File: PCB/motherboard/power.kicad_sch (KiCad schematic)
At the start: 0 parts

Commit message: started power schematic of pcb
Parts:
- added C1, C2, C3: C, symbol Device:C
- added C4: 100n, symbol Device:C
- added C5: 10u, symbol Device:C
- added L1: L, symbol Device:L
- added R1, R2, R3, R4, R6: R, symbol Device:R
- added U1: TPS54140ADGQR, DGQ10_1P88X1P57_TEX, symbol tps54140:TPS54140ADGQR
- added U2: PTPS259830LNRGER, VQFN24_RGE_TEX, symbol tps25983:PTPS259830LNRGER
- added U3: AP2112K-3.3TRG1, SOT_RG1_DIO, symbol AP2112K-3.3TRG1:AP2112K-3.3TRG1
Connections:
- new net: L1.1, U1.10 (PH)
- new net: R3.2, R4.1, U2.12 (OVLO)
- new net: C1.1, U2.7 (ITIMER)
- new net: R6.1, U2.8 (ILIM)
- new net: R2.2, R3.1, U2.6 (EN/UVLO)
- new net: C3.1, U2.15 (DVDT/_BGATE)
- new net: C2.1, U2.10 (RETRY_DLY)
- new net +24V: C5.1, U1.2 (VIN), U2.17 (OUT), U2.18 (OUT), U2.19 (OUT), U2.20 (OUT), U2.21 (OUT), U2.22 (OUT), U2.23 (OUT), U2.24 (OUT)
- new net +24V_UNPROTECTED: C4.1, R2.1, U2.1 (IN), U2.16 (IN), U2.2 (IN), U2.25 (IN), U2.3 (IN)
- new net +3.3V: U3.5 (VOUT)
- new net +5V: L1.2, U3.1 (VIN)
- new net GND: C1.2, C2.2, C3.2, C4.2, C5.2, R1.2, R4.2, R6.2, U1.9 (GND), U2.11 (NRETRY), U2.14 (GND), U2.26 (GND), U2.4 (GND), U2.5 (GND), U3.2 (GND)
- new net IMON: R1.1, U2.9 (IMON)
- new net PG_EFUSE: U2.13 (PG)
- no-connect marks 0 -> 1
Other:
- note added: "BUCK 24V TO 5V"
- note added: "EFUSE"
- note added: "LDO 5V to 3V3"

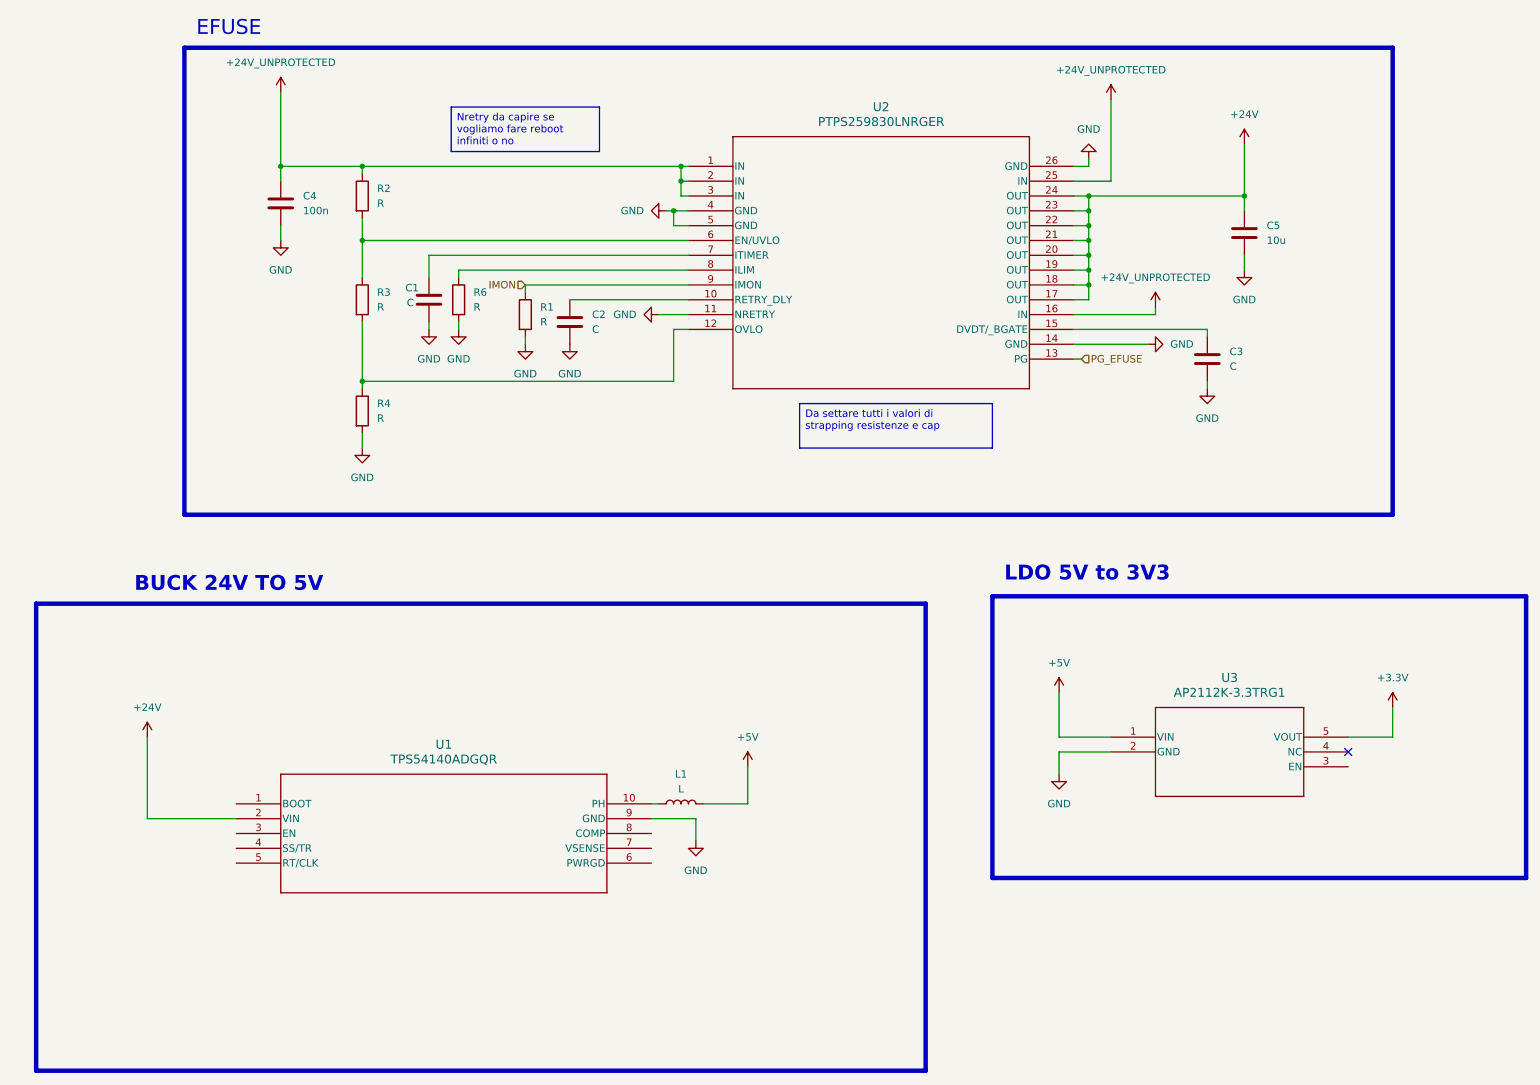
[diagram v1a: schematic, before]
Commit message: updated sch power
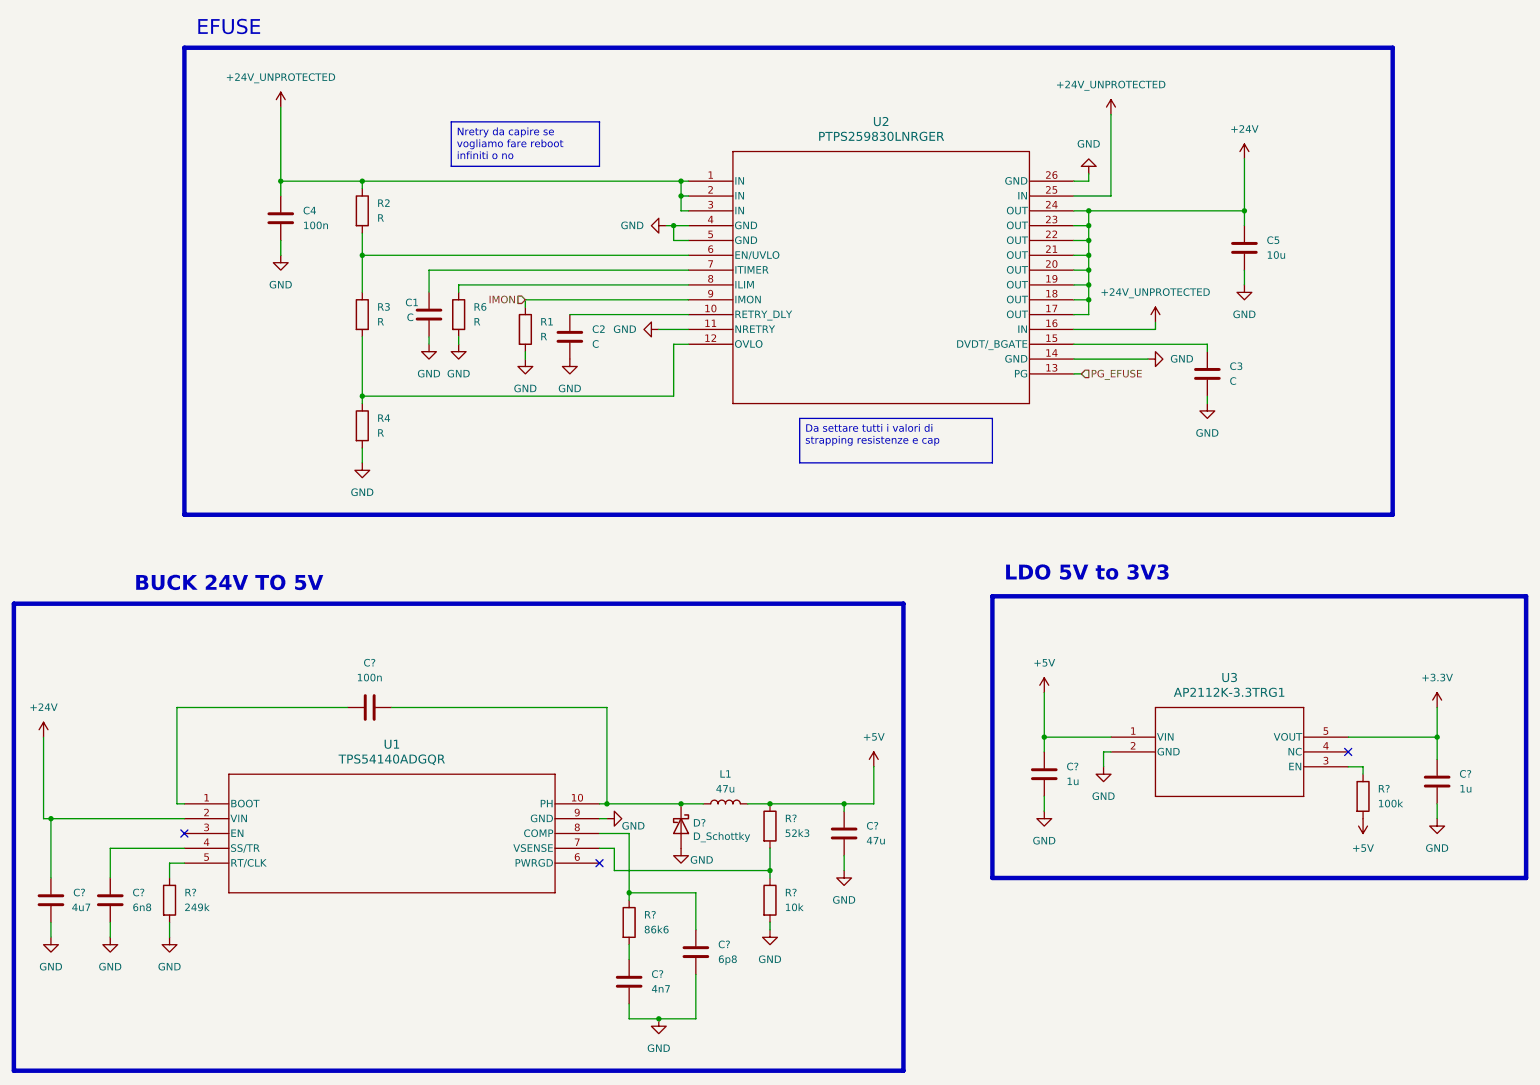
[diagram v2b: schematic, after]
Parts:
- added C?: 6n8, symbol Device:C
- added C?: 4u7, symbol Device:C
- added C?: 100n, symbol Device:C
- added C? (x2): 1u, symbol Device:C
- added C?: 47u, symbol Device:C
- added C?: 6p8, symbol Device:C
- added C?: 4n7, symbol Device:C
- added D?: D_Schottky, symbol Device:D_Schottky
- added R?: 100k, symbol Device:R
- added R?: 86k6, symbol Device:R
- added R?: 52k3, symbol Device:R
- added R?: 10k, symbol Device:R
- added R?: 249k, symbol Device:R
- L1: value L -> 47u
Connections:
- net +24V: now also C?.1
- net +3.3V: now also C?.1
- net +5V: now also C?.1, C?.1, R?.1, R?.2
- net GND: now also C?.2, C?.2, C?.2, C?.2, C?.2, C?.2, C?.2, D?.2 (A), R?.2, R?.2
- net at U1.1 (BOOT): now also C?.1
- net at L1.1, U1.10 (PH): now also C?.2, D?.1 (K)
- net at U1.4 (SS/TR): now also C?.1
- net at U1.5 (RT/CLK): now also R?.1
- net at U1.7 (VSENSE): now also R?.1, R?.2
- net at U1.8 (COMP): now also C?.1, R?.1
- net at U3.3 (EN): now also R?.1
- new net: C?.1, R?.2
- no-connect marks 1 -> 3
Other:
- moved on the sheet: C1, C2, C3, C4, C5, L1, R1, R2, R3, R4, R6, U1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
